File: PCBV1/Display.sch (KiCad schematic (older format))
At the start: 11 parts, among them J3 QSH-030-01-F-D-A-K-TR

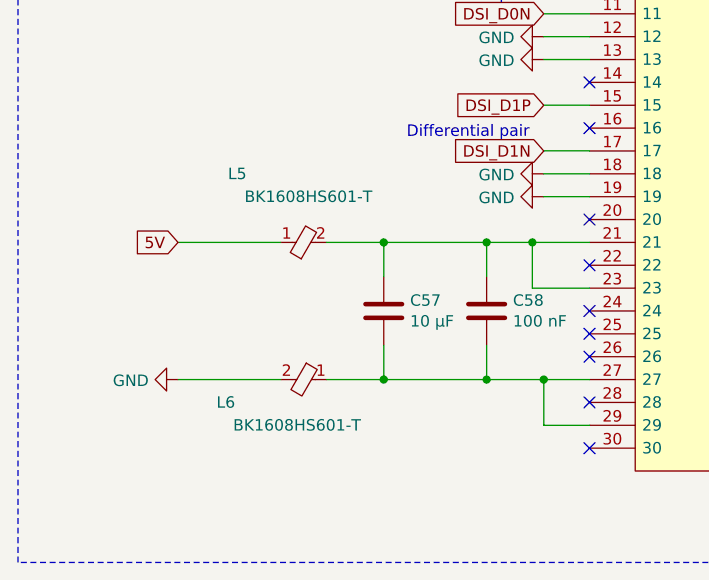
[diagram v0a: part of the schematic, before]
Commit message: Changed ferrite beads to ones with adequate max currents. Changed JTAG connector to 20-pin standard. Minor PCB fixes.
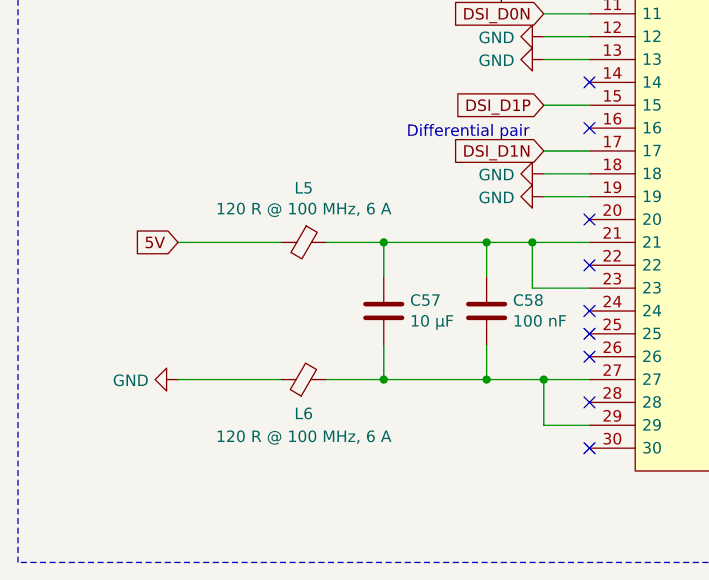
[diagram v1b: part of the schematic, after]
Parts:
- removed L5, L6: BK1608HS601-T, BEADC1608X95N, symbol SamacSys_Parts:BK1608HS601-T
- added L5, L6: 120 R @ 100 MHz, 6 A, Inductor_SMD:L_0805_2012Metric, symbol Device:Ferrite_Bead_Small
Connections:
- net 5V: now also L5.2
- net GND: now also L6.1
- net at C57.1, C58.1, J3.21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: now also L5.1
- net at C57.2, C58.2, J3.27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: now also L6.2
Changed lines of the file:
@@
-$EndComp
-$Comp
-L SamacSys_Parts:BK1608HS601-T L5
-U 1 1 5F47BDA9
-P 3250 4100
-F 0 "L5" H 3100 4400 50  0000 R CNN
-F 1 "BK1608HS601-T" H 3650 4300 50  0000 R CNN
-F 2 "BEADC1608X95N" H 3900 4200 50  0001 L CNN
-F 3 "https://componentsearchengine.com/Datasheets/2/BK1608HS601-T.pdf" H 3900 4100 50  0001 L CNN
-F 4 "TAIYO YUDEN - BK1608HS601-T - FERRITE BEAD, 0.45OHM, 350mA, 0603" H 3900 4000 50  0001 L CNN "Description"
-F 5 "0.95" H 3900 3900 50  0001 L CNN "Height"
-F 6 "963-BK1608HS601-T" H 3900 3800 50  0001 L CNN "Mouser Part Number"
-F 7 "https://www.mouser.co.uk/ProductDetail/Taiyo-Yuden/BK1608HS601-T?qs=I6KAKw0tg2yRykYpbtkrDg%3D%3D" H 3900 3700 50  0001 L CNN "Mouser Price/Stock"
-F 8 "TAIYO YUDEN" H 3900 3600 50  0001 L CNN "Manufacturer_Name"
-F 9 "BK1608HS601-T" H 3900 3500 50  0001 L CNN "Manufacturer_Part_Number"
-	1    3250 4100
-	1    0    0    -1
-$EndComp
-$Comp
-L SamacSys_Parts:BK1608HS601-T L6
-U 1 1 5F47D0CA
-P 3450 4700
-F 0 "L6" H 3850 4800 50  0000 L CNN
-F 1 "BK1608HS601-T" H 3300 4900 50  0000 L CNN
-F 2 "BEADC1608X95N" H 4100 4800 50  0001 L CNN
-F 3 "https://componentsearchengine.com/Datasheets/2/BK1608HS601-T.pdf" H 4100 4700 50  0001 L CNN
-F 4 "TAIYO YUDEN - BK1608HS601-T - FERRITE BEAD, 0.45OHM, 350mA, 0603" H 4100 4600 50  0001 L CNN "Description"
-F 5 "0.95" H 4100 4500 50  0001 L CNN "Height"
-F 6 "963-BK1608HS601-T" H 4100 4400 50  0001 L CNN "Mouser Part Number"
-F 7 "https://www.mouser.co.uk/ProductDetail/Taiyo-Yuden/BK1608HS601-T?qs=I6KAKw0tg2yRykYpbtkrDg%3D%3D" H 4100 4300 50  0001 L CNN "Mouser Price/Stock"
-F 8 "TAIYO YUDEN" H 4100 4200 50  0001 L CNN "Manufacturer_Name"
-F 9 "BK1608HS601-T" H 4100 4100 50  0001 L CNN "Manufacturer_Part_Number"
-	1    3450 4700
-	-1   0    0    1
 $EndComp
 $Comp
@@
 Wire Notes Line
 	2100 5500 2100 1750
+$Comp
+L Device:Ferrite_Bead_Small L5
+U 1 1 5F971D7C
+P 3350 4100
+F 0 "L5" V 3113 4100 50  0000 C CNN
+F 1 "120 R @ 100 MHz, 6 A" V 3204 4100 50  0000 C CNN
+F 2 "Inductor_SMD:L_0805_2012Metric" V 3280 4100 50  0001 C CNN
+F 3 "https://www.mouser.dk/ProductDetail/Fair-Rite/2508051217Y6?qs=paL1wOLBYNdSlNbDsszWbQ%3D%3D" H 3350 4100 50  0001 C CNN
+F 4 "250805127Y6" V 3350 4100 50  0001 C CNN "Name"
+	1    3350 4100
+	0    1    1    0
+$EndComp
+$Comp
+L Device:Ferrite_Bead_Small L6
+U 1 1 5F973F43
+P 3350 4700
+F 0 "L6" V 3200 4700 50  0000 C CNN
+F 1 "120 R @ 100 MHz, 6 A" V 3100 4700 50  0000 C CNN
+F 2 "Inductor_SMD:L_0805_2012Metric" V 3280 4700 50  0001 C CNN
+F 3 "https://www.mouser.dk/ProductDetail/Fair-Rite/2508051217Y6?qs=paL1wOLBYNdSlNbDsszWbQ%3D%3D" H 3350 4700 50  0001 C CNN
+F 4 "250805127Y6" V 3350 4700 50  0001 C CNN "Name"
+	1    3350 4700
+	0    -1   -1   0
+$EndComp
 $EndSCHEMATC

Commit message: Added new JTAG/UART header with connections for STLink V3. Moved from SamacSys to personal GitHub-based library.
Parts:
- removed J3: QSH-030-01-F-D-A-K-TR, QSH-030-01-F-D-A, symbol SamacSys_Parts:QSH-030-01-F-D-A-K-TR
- added J3: QSH-030-01-F-D-A-K-TR, Personal_Misc:QSH-030-01-F-D-A, symbol Personal_Misc:QSH-030-01-F-D-A-K-TR
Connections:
- net 3V3: now also J3.36
- net DSI_CKN: now also J3.5
- net DSI_CKP: now also J3.3
- net DSI_D0N: now also J3.11
- net DSI_D0P: now also J3.9
- net DSI_D1N: now also J3.17
- net DSI_D1P: now also J3.15
- net DSI_RESET: now also J3.57
- net DSI_TE: now also J3.49
- net GND: now also J3.1, J3.12, J3.13, J3.18, J3.19, J3.6, J3.7
- net I2C1_SCL: now also J3.44
- net I2C1_SDA: now also J3.40
- net LCD_BL_CTRL: now also J3.53
- net LCD_INT: now also J3.4
- net at C57.1, C58.1, L5.1: now also J3.21, J3.23
- net at C57.2, C58.2, L6.2: now also J3.27, J3.29
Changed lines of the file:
@@
 Comment4 ""
 $EndDescr
-$Comp
-L SamacSys_Parts:QSH-030-01-F-D-A-K-TR J3
-U 1 1 5F5B637B
-P 4600 2100
-F 0 "J3" H 5050 2365 50  0000 C CNN
-F 1 "QSH-030-01-F-D-A-K-TR" H 5050 2274 50  0000 C CNN
-F 2 "QSH-030-01-F-D-A" H 5350 2200 50  0001 L CNN
-F 3 "http://suddendocs.samtec.com/prints/qsh-xxx-01-x-d-xxx-mkt.pdf" H 5350 2100 50  0001 L CNN
-F 4 ".5MM DOUBLE ROW MI SOCKET ASSEMB" H 5350 2000 50  0001 L CNN "Description"
-F 5 "" H 5350 1900 50  0001 L CNN "Height"
-F 6 "200-QSH03001FDAKTR" H 5350 1800 50  0001 L CNN "Mouser Part Number"
-F 7 "https://www.mouser.co.uk/ProductDetail/Samtec/QSH-030-01-F-D-A-K-TR?qs=rU5fayqh%252BE1MoJ3Rko0Mxw%3D%3D" H 5350 1700 50  0001 L CNN "Mouser Price/Stock"
-F 8 "SAMTEC" H 5350 1600 50  0001 L CNN "Manufacturer_Name"
-F 9 "QSH-030-01-F-D-A-K-TR" H 5350 1500 50  0001 L CNN "Manufacturer_Part_Number"
-	1    4600 2100
-	1    0    0    -1
-$EndComp
 Text GLabel 2800 4100 0    50   Input ~ 0
 5V
@@
 	0    -1   -1   0
 $EndComp
+$Comp
+L Personal_Misc:QSH-030-01-F-D-A-K-TR J3
+U 1 1 5FBE6AAD
+P 4600 2100
+F 0 "J3" H 5050 2365 50  0000 C CNN
+F 1 "QSH-030-01-F-D-A-K-TR" H 5050 2274 50  0000 C CNN
+F 2 "Personal_Misc:QSH-030-01-F-D-A" H 5350 2200 50  0001 L CNN
+F 3 "http://suddendocs.samtec.com/prints/qsh-xxx-01-x-d-xxx-mkt.pdf" H 5350 2100 50  0001 L CNN
+F 4 ".5MM DOUBLE ROW MI SOCKET ASSEMB" H 5350 2000 50  0001 L CNN "Description"
+F 5 "200-QSH03001FDAKTR" H 5350 1800 50  0001 L CNN "Mouser Part Number"
+F 6 "https://www.mouser.co.uk/ProductDetail/Samtec/QSH-030-01-F-D-A-K-TR?qs=rU5fayqh%252BE1MoJ3Rko0Mxw%3D%3D" H 5350 1700 50  0001 L CNN "Mouser Price/Stock"
+F 7 "SAMTEC" H 5350 1600 50  0001 L CNN "Manufacturer_Name"
+F 8 "QSH-030-01-F-D-A-K-TR" H 5350 1500 50  0001 L CNN "Manufacturer_Part_Number"
+	1    4600 2100
+	1    0    0    -1
+$EndComp
 $EndSCHEMATC
